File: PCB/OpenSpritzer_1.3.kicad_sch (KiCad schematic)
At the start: 26 parts, among them J1 to Foot Pedal, J2 Barrel_Jack, J3 to Solenoid, J4 to TTL pulse generator, J5 on/off switch, Q1 Q_NPN_Darlington_EBC, SW1 SW_DPDT_x2, U1 LM2596S-12

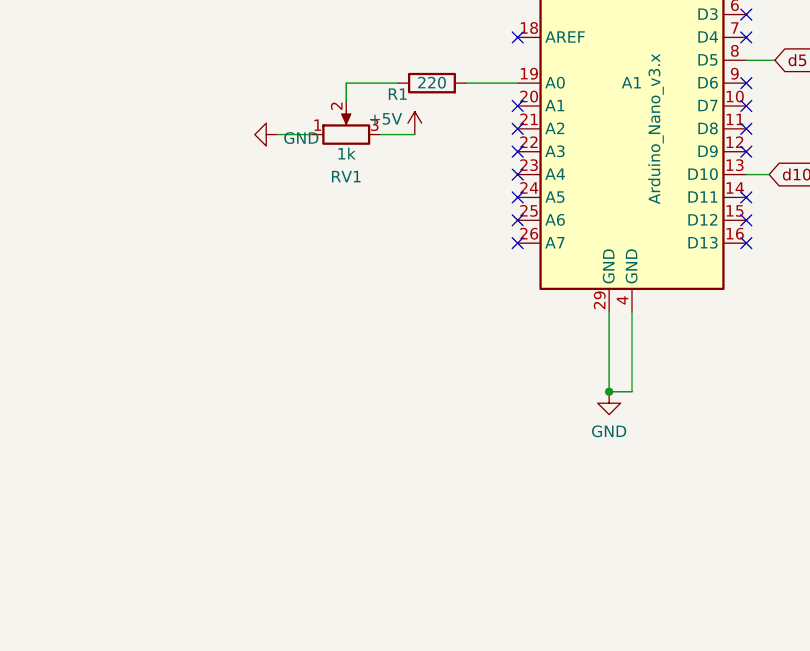
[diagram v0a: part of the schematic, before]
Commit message: add i2c pin layout
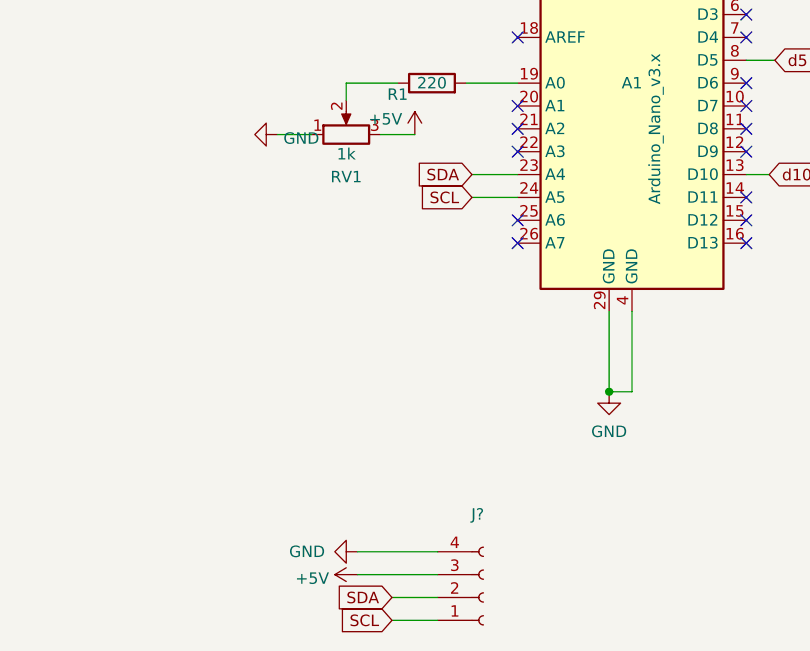
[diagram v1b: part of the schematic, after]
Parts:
- added J?: (no value), symbol Connector:Conn_01x04_Female
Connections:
- net +5V: now also J?.3 (Pin_3)
- net GND: now also J?.4 (Pin_4)
- net SDA: now reaches A1.23 (A4)
- net SDA: now also J?.2 (Pin_2)
- net SCL: now reaches A1.24 (A5)
- net SCL: now also J?.1 (Pin_1)
- no-connect marks 22 -> 20
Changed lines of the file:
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@@
   (no_connect (at 132.08 73.66))
   (no_connect (at 157.48 101.6))
-  (no_connect (at 132.08 101.6))
   (no_connect (at 157.48 76.2))
   (no_connect (at 132.08 93.98))
   (no_connect (at 132.08 76.2))
   (no_connect (at 157.48 81.28))
-  (no_connect (at 132.08 99.06))
   (no_connect (at 142.24 63.5))
   (no_connect (at 157.48 93.98))
@@
     (stroke (width 0) (type default) (color 0 0 0 0))
   )
+  (wire (pts (xy 127 101.6) (xy 132.08 101.6))
+    (stroke (width 0) (type default) (color 0 0 0 0))
+  )
   (wire (pts (xy 33.655 36.195) (xy 34.925 36.195))
     (stroke (width 0) (type default) (color 0 0 0 0))
@@
     (stroke (width 0) (type default) (color 0 0 0 0))
   )
+  (wire (pts (xy 114.3 140.97) (xy 123.19 140.97))
+    (stroke (width 0) (type default) (color 0 0 0 0))
+  )
   (wire (pts (xy 215.9 73.66) (xy 219.71 73.66))
     (stroke (width 0) (type default) (color 0 0 0 0))
@@
     (stroke (width 0) (type default) (color 0 0 0 0))
   )
+  (wire (pts (xy 118.11 146.05) (xy 123.19 146.05))
+    (stroke (width 0) (type default) (color 0 0 0 0))
+  )
   (wire (pts (xy 32.385 43.815) (xy 22.225 43.815))
     (stroke (width 0) (type default) (color 0 0 0 0))
@@
     (stroke (width 0) (type default) (color 0 0 0 0))
   )
+  (wire (pts (xy 118.11 148.59) (xy 123.19 148.59))
+    (stroke (width 0) (type default) (color 0 0 0 0))
+  )
   (wire (pts (xy 142.24 114.3) (xy 142.24 123.19))
     (stroke (width 0) (type default) (color 0 0 0 0))
@@
     (stroke (width 0) (type default) (color 0 0 0 0))
   )
+  (wire (pts (xy 114.3 143.51) (xy 123.19 143.51))
+    (stroke (width 0) (type default) (color 0 0 0 0))
+  )
   (wire (pts (xy 22.225 36.195) (xy 23.495 36.195))
     (stroke (width 0) (type default) (color 0 0 0 0))
@@
     (stroke (width 0) (type default) (color 0 0 0 0))
   )
+  (wire (pts (xy 127 99.06) (xy 132.08 99.06))
+    (stroke (width 0) (type default) (color 0 0 0 0))
+  )
   (wire (pts (xy 64.135 41.275) (xy 66.675 41.275))
     (stroke (width 0) (type default) (color 0 0 0 0))
@@
   (wire (pts (xy 201.93 83.82) (xy 219.71 83.82))
     (stroke (width 0) (type default) (color 0 0 0 0))
+  )
+  (global_label "SCL" (shape input) (at 127 101.6 180) (fields_autoplaced)
+    (effects (font (size 1.27 1.27)) (justify right))
+    (property "Intersheet References" "${INTERSHEET_REFS}" (id 0) (at 121.1682 101.5206 0)
+      (effects (font (size 1.27 1.27)) (justify right) hide)
+    )
+  )
+  (global_label "SDA" (shape input) (at 127 99.06 180) (fields_autoplaced)
+    (effects (font (size 1.27 1.27)) (justify right))
+    (property "Intersheet References" "${INTERSHEET_REFS}" (id 0) (at 121.1077 98.9806 0)
+      (effects (font (size 1.27 1.27)) (justify right) hide)
+    )
   )
   (global_label "d5" (shape input) (at 163.83 76.2 180) (fields_autoplaced)
     (effects (font (size 1.27 1.27)) (justify right))
     (property "Intersheet References" "${INTERSHEET_REFS}" (id 0) (at 159.1472 76.2794 0)
+      (effects (font (size 1.27 1.27)) (justify right) hide)
+    )
+  )
+  (global_label "SDA" (shape input) (at 118.11 146.05 180) (fields_autoplaced)
+    (effects (font (size 1.27 1.27)) (justify right))
+    (property "Intersheet References" "${INTERSHEET_REFS}" (id 0) (at 112.2177 145.9706 0)
+      (effects (font (size 1.27 1.27)) (justify right) hide)
+    )
+  )
+  (global_label "SCL" (shape input) (at 118.11 148.59 180) (fields_autoplaced)
+    (effects (font (size 1.27 1.27)) (justify right))
+    (property "Intersheet References" "${INTERSHEET_REFS}" (id 0) (at 112.2782 148.5106 0)
       (effects (font (size 1.27 1.27)) (justify right) hide)
     )
@@
     (pin "2")
     (pin "3")
+    (pin "4")
+    (pin "5")
+    (pin "6")
   )
   (symbol (lib_id "Switch:SW_DPDT_x2") (at 170.18 73.66 0) (mirror y) (unit 2)
@@
       (effects (font (size 1.27 1.27)) hide)
     )
+    (pin "1")
+    (pin "2")
+    (pin "3")
     (pin "4")
     (pin "5")
@@
     (pin "1")
   )
+  (symbol (lib_id "power:+5V") (at 114.3 143.51 90) (unit 1)
+    (in_bom yes) (on_board yes) (fields_autoplaced)
+    (property "Reference" "#PWR?" (id 0) (at 118.11 143.51 0)
+      (effects (font (size 1.27 1.27)) hide)
+    )
+    (property "Value" "+5V" (id 1) (at 111.1251 143.9438 90)
+      (effects (font (size 1.27 1.27)) (justify left))
+    )
+    (property "Footprint" "" (id 2) (at 114.3 143.51 0)
+      (effects (font (size 1.27 1.27)) hide)
+    )
+    (property "Datasheet" "" (id 3) (at 114.3 143.51 0)
+      (effects (font (size 1.27 1.27)) hide)
+    )
+    (pin "1")
+  )
   (symbol (lib_id "power:GND") (at 228.6 86.995 0) (unit 1)
     (in_bom yes) (on_board yes) (fields_autoplaced)
@@
     )
     (property "Datasheet" "" (id 3) (at 228.6 86.995 0)
+      (effects (font (size 1.27 1.27)) hide)
+    )
+    (pin "1")
+  )
+  (symbol (lib_id "power:GND") (at 114.3 140.97 270) (unit 1)
+    (in_bom yes) (on_board yes)
+    (property "Reference" "#PWR?" (id 0) (at 107.95 140.97 0)
+      (effects (font (size 1.27 1.27)) hide)
+    )
+    (property "Value" "GND" (id 1) (at 106.68 140.97 90)
+      (effects (font (size 1.27 1.27)) (justify left))
+    )
+    (property "Footprint" "" (id 2) (at 114.3 140.97 0)
+      (effects (font (size 1.27 1.27)) hide)
+    )
+    (property "Datasheet" "" (id 3) (at 114.3 140.97 0)
       (effects (font (size 1.27 1.27)) hide)
     )
@@
     (pin "1")
   )
+  (symbol (lib_id "Connector:Conn_01x04_Female") (at 128.27 146.05 0) (mirror x) (unit 1)
+    (in_bom yes) (on_board yes) (fields_autoplaced)
+    (property "Reference" "J?" (id 0) (at 127.635 136.813 0))
+    (property "Value" "" (id 1) (at 127.635 139.3499 0))
+    (property "Footprint" "" (id 2) (at 128.27 146.05 0)
+      (effects (font (size 1.27 1.27)) hide)
+    )
+    (property "Datasheet" "~" (id 3) (at 128.27 146.05 0)
+      (effects (font (size 1.27 1.27)) hide)
+    )
+    (pin "1")
+    (pin "2")
+    (pin "3")
+    (pin "4")
+  )
   (symbol (lib_id "power:GND") (at 65.405 112.395 90) (unit 1)
     (in_bom yes) (on_board yes) (fields_autoplaced)
@@
       (reference "#PWR019") (unit 1) (value "+24V") (footprint "")
     )
+    (path "/773f4a37-ba83-4e69-a1c5-439d64aa2155"
+      (reference "#PWR?") (unit 1) (value "+5V") (footprint "")
+    )
+    (path "/8f37976d-7277-408d-b960-1ce55db355b4"
+      (reference "#PWR?") (unit 1) (value "GND") (footprint "")
+    )
     (path "/00000000-0000-0000-0000-00005b597e17"
       (reference "A1") (unit 1) (value "Arduino_Nano_v3.x") (footprint "Modules:Arduino_Nano_WithMountingHoles")
@@
       (reference "J5") (unit 1) (value "on/off switch") (footprint "")
     )
+    (path "/ddb83956-0781-4967-adf3-cb27a82b32ef"
+      (reference "J?") (unit 1) (value "SSD1306_screen") (footprint "")
+    )
     (path "/00000000-0000-0000-0000-00005b643034"

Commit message: update footprints
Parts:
- A1: footprint Modules:Arduino_Nano_WithMountingHoles -> Module:Arduino_Nano
- C1: footprint (none) -> Capacitor_THT:CP_Radial_D8.0mm_P3.50mm
- C2: footprint (none) -> Capacitor_THT:CP_Radial_D6.3mm_P2.50mm
- C3: footprint (none) -> Capacitor_THT:C_Disc_D7.5mm_W4.4mm_P5.00mm
- D3: footprint (none) -> Diode_THT:D_DO-27_P15.24mm_Horizontal
- D5, J2, J5: footprint (none) -> Connector_JST:JST_XH_B2B-XH-A_1x02_P2.50mm_Vertical
- J1: value to Foot Pedal -> from Foot Pedal
- J4: value to TTL pulse generator -> from TTL pulse generator
- J6: renamed from J?; value (none) -> SSD1306_screen; footprint (none) -> Connector_JST:JST_XH_B4B-XH-A_1x04_P2.50mm_Vertical
- R1, R2, R3, R4, R5, R6: footprint Resistors_THT:R_Axial_DIN0204_L3.6mm_D1.6mm_P2.54mm_Vertical -> Resistor_THT:R_Axial_DIN0414_L11.9mm_D4.5mm_P15.24mm_Horizontal
- R7, RV1: footprint (none) -> Resistor_THT:R_Axial_DIN0414_L11.9mm_D4.5mm_P15.24mm_Horizontal
- SW1: footprint Buttons_Switches_THT:SW_CuK_JS202011AQN_DPDT_Angled -> Button_Switch_THT:SW_Push_2P2T_Vertical_E-Switch_800UDP8P1A1M6

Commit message: update new board
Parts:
- removed J2: Barrel_Jack, Connector_JST:JST_XH_B2B-XH-A_1x02_P2.50mm_Vertical, symbol Connector:Barrel_Jack
- removed J5: on/off switch, Connector_JST:JST_XH_B2B-XH-A_1x02_P2.50mm_Vertical, symbol Connector:Conn_01x02_Female
- added H1, H2, H3, H4: MountingHole, MountingHole:MountingHole_3.2mm_M3_DIN965, symbol Mechanical:MountingHole
- added J2: barrel_jack, Connector_BarrelJack:BarrelJack_GCT_DCJ200-10-A_Horizontal, symbol Connector:Conn_01x03_Female
- added SW2: SW_DPDT_x2, Button_Switch_THT:SW_Push_2P2T_Vertical_E-Switch_800UDP8P1A1M6, symbol Switch:SW_DPDT_x2
- C1: value C_Polarized -> 680µF
- C2: value C_Polarized -> 220µF
- D1: footprint LEDs:LED_D5.0mm -> LED_THT:LED_D5.0mm_Horizontal_O1.27mm_Z15.0mm
- D5: footprint Connector_JST:JST_XH_B2B-XH-A_1x02_P2.50mm_Vertical -> LED_THT:LED_D5.0mm_Horizontal_O1.27mm_Z15.0mm
- Q1: footprint Transistors_OldSowjetAera:OldSowjetaera_Transistor_Type-I_BigPads -> Package_TO_SOT_THT:TO-92L_Wide
- RV1: footprint Resistor_THT:R_Axial_DIN0414_L11.9mm_D4.5mm_P15.24mm_Horizontal -> Connector_JST:JST_XH_B3B-XH-A_1x03_P2.50mm_Vertical
- U1: footprint TO_SOT_Packages_THT:TO-220-5_Vertical_StaggeredType1 -> Package_TO_SOT_THT:TO-220-5_P3.4x3.7mm_StaggerOdd_Lead3.8mm_Vertical
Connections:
- net +24V: now also J2.1 (Pin_1), SW2.1 (A); no longer C1.1, D3.1 (K), D5.2 (A), J3.1 (Pin_1), U1.1 (VIN)
- net +5V: now also J1.1 (Pin_1); no longer J1.2 (Pin_2)
- net GND: now also J2.2 (Pin_2), SW2.3 (C), SW2.4 (A), SW2.5 (B), SW2.6 (C)
- net at R3.1, R5.1: now also J1.2 (Pin_2); no longer J1.1 (Pin_1)
- new net to_buck_conv: C1.1, D3.1 (K), D5.2 (A), J3.1 (Pin_1), SW2.2 (B), U1.1 (VIN)
- no-connect marks 20 -> 21
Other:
- moved on the sheet: D5, R7
